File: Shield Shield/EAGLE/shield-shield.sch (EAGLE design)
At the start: 19 parts, among them IC1 MC33269D-5.0, J1 POWER_JACKSLT, U1 TXB0108PWR, U2 TXB0108PWR

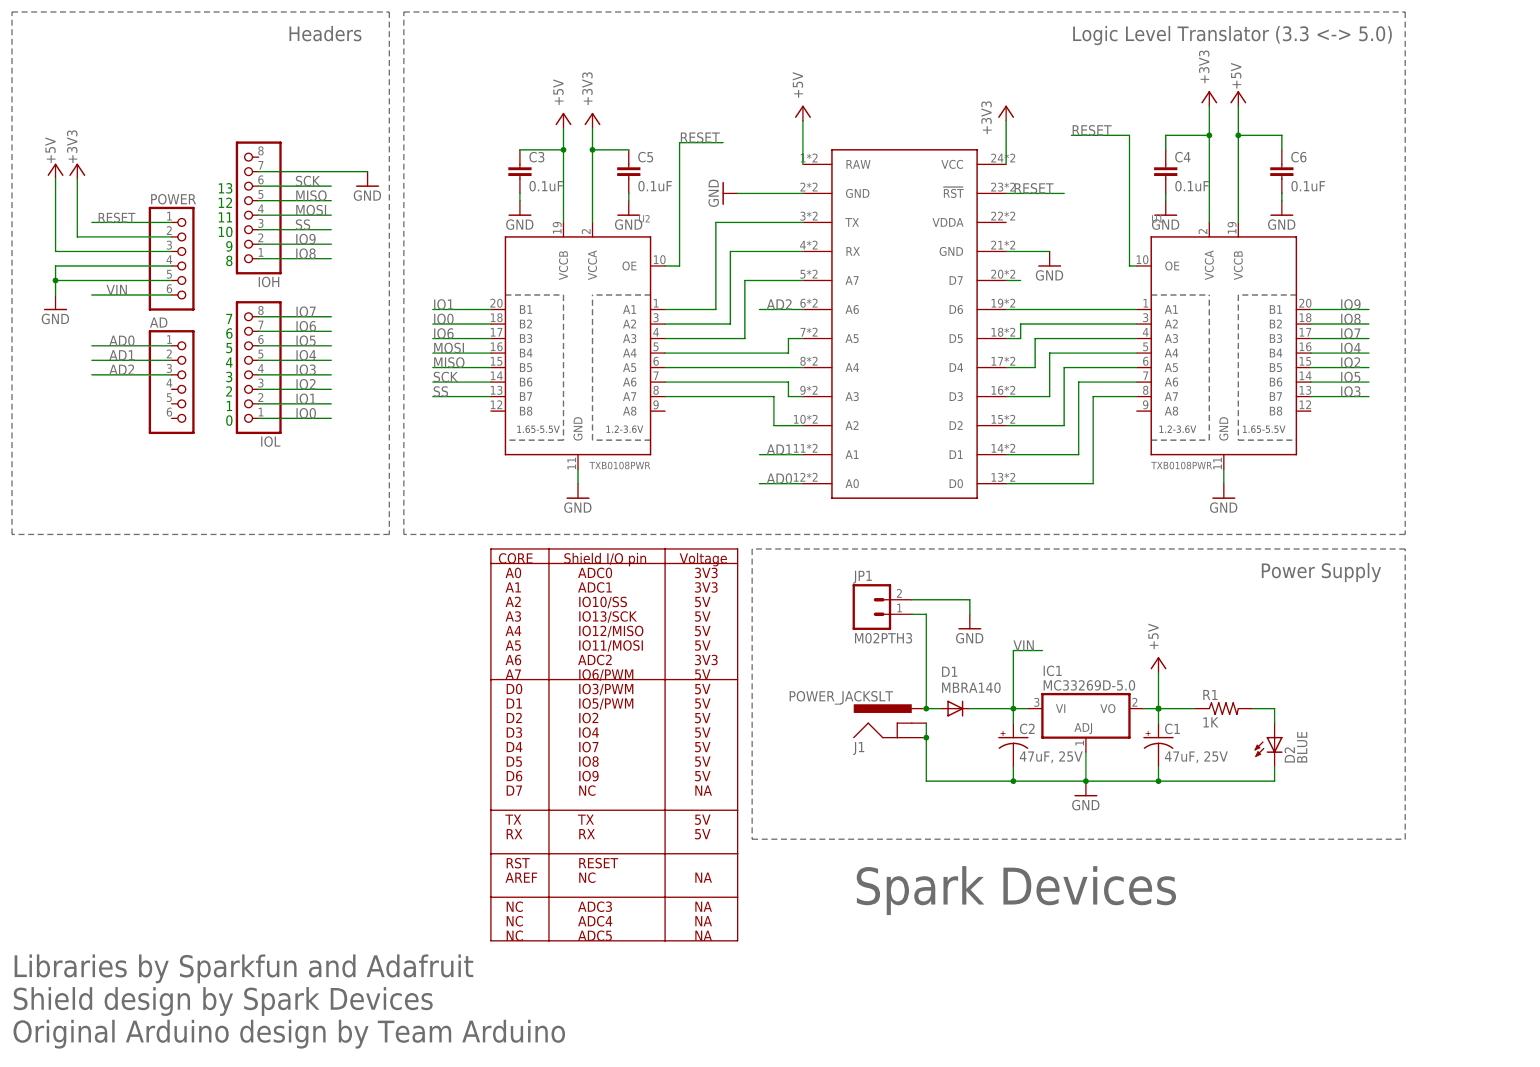
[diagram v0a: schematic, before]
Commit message: updated shield BOMs and boards
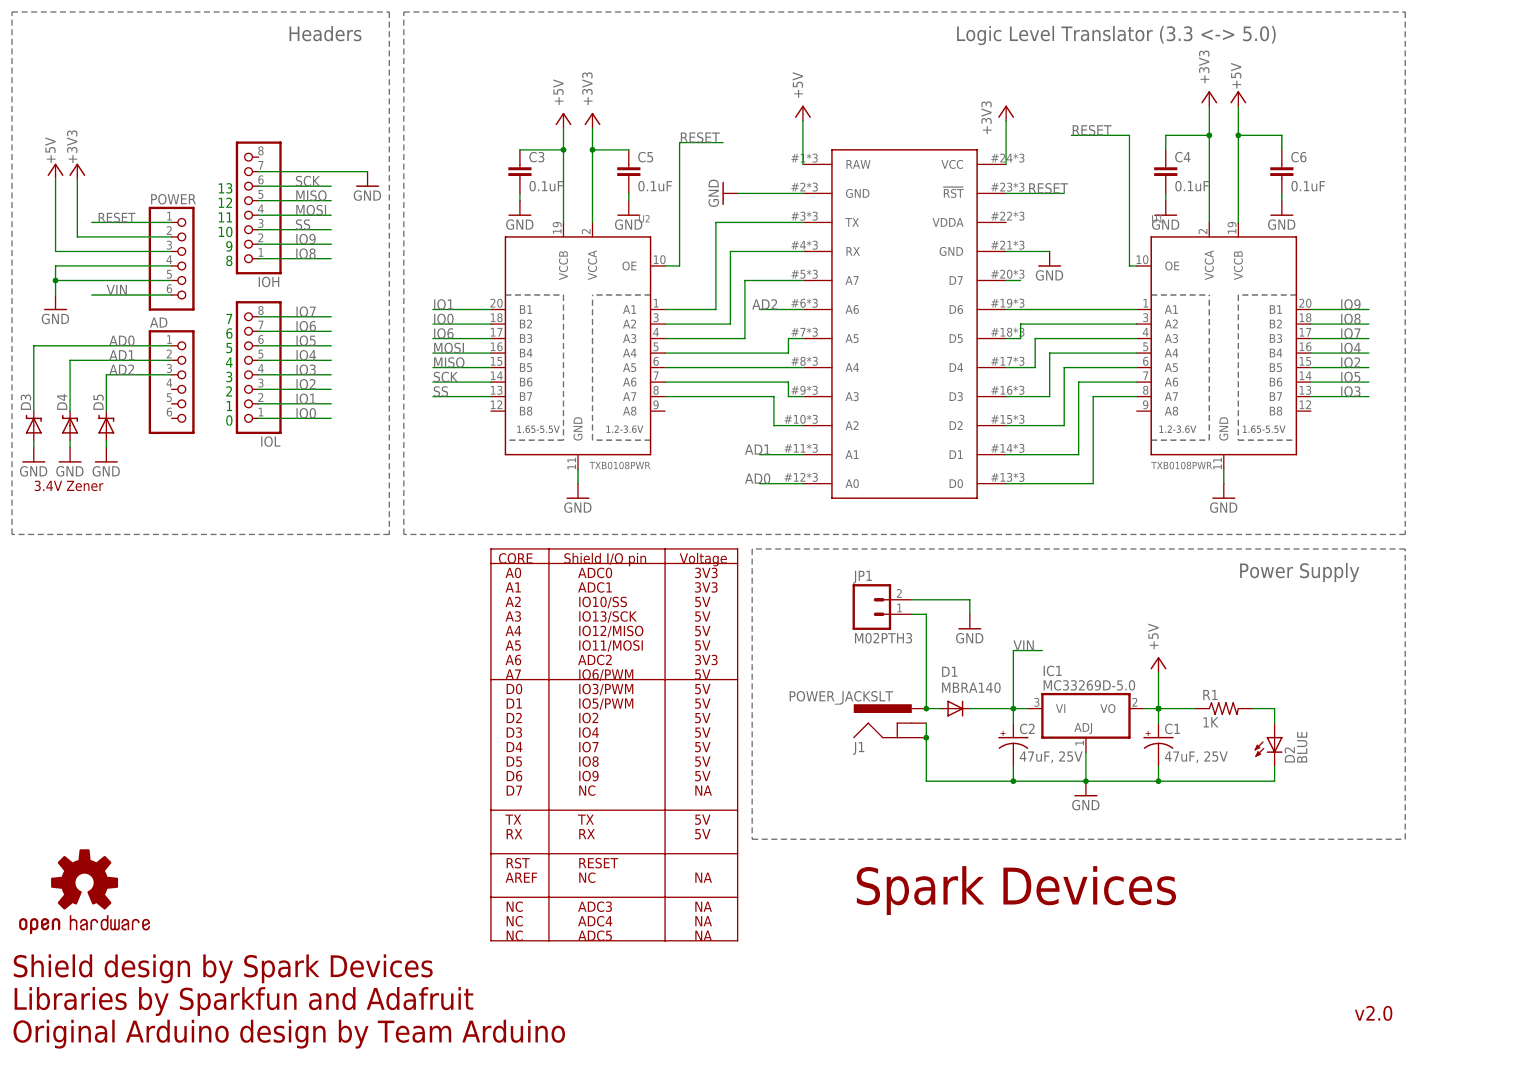
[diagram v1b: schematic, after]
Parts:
- added D3, D4, D5: DIODE-ZENER-BZT52, SparkFun-DiscreteSemi:DIODE-ZENER-BZT52
- added LOGO1: OSHW-LOGOM, Spark:OSHW-LOGOM
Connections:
- net AD0: now also D3.C
- net AD1: now also D4.C
- net AD2: now also D5.C
- net GND: now also D3.A, D4.A, D5.A
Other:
- note added: "3.4V Zener"
- note added: "Shield design by Spark Devices Libraries by Sparkfun and Adafruit Original Arduino design by Team Arduino"
- note added: "v2.0"
- note removed: "Libraries by Sparkfun and Adafruit Shield design by Spark Devices Original Arduino design by Team Arduino"
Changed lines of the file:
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@@
 <layer number="95" name="Names" color="7" fill="1" visible="yes" active="yes"/>
 <layer number="96" name="Values" color="7" fill="1" visible="yes" active="yes"/>
-<layer number="97" name="Info" color="7" fill="1" visible="no" active="yes"/>
+<layer number="97" name="Info" color="7" fill="1" visible="yes" active="yes"/>
 <layer number="98" name="Guide" color="6" fill="1" visible="no" active="yes"/>
 <layer number="100" name="Muster" color="7" fill="1" visible="no" active="yes"/>
@@
 <layer number="112" name="tSilk" color="7" fill="1" visible="yes" active="yes"/>
 <layer number="116" name="Patch_BOT" color="7" fill="1" visible="no" active="yes"/>
-<layer number="121" name="_tsilk" color="7" fill="1" visible="no" active="yes"/>
+<layer number="121" name="_tsilk" color="7" fill="1" visible="yes" active="yes"/>
 <layer number="122" name="_bsilk" color="7" fill="1" visible="no" active="yes"/>
 <layer number="123" name="tTestmark" color="7" fill="1" visible="no" active="yes"/>
@@
 <part name="JP1" library="SparkFun-Connectors" deviceset="M02" device="PTH3"/>
 <part name="GND11" library="supply1" deviceset="GND" device=""/>
+<part name="LOGO1" library="Spark" deviceset="OSHW-LOGO" device="M"/>
+<part name="D3" library="SparkFun-DiscreteSemi" deviceset="DIODE-ZENER" device="-BZT52"/>
+<part name="D4" library="SparkFun-DiscreteSemi" deviceset="DIODE-ZENER" device="-BZT52"/>
+<part name="D5" library="SparkFun-DiscreteSemi" deviceset="DIODE-ZENER" device="-BZT52"/>
+<part name="GND12" library="supply1" deviceset="GND" device=""/>
+<part name="GND13" library="supply1" deviceset="GND" device=""/>
+<part name="GND15" library="supply1" deviceset="GND" device=""/>
 </parts>
 <sheets>
@@
 <text x="41.275" y="148.59" size="1.778" layer="91" rot="MR0">12</text>
 <text x="41.275" y="151.13" size="1.778" layer="91" rot="MR0">13</text>
-<text x="149.86" y="26.67" size="6.4516" layer="95">Spark Devices</text>
+<text x="149.86" y="26.67" size="6.4516" layer="94" font="vector">Spark Devices</text>
 <wire x1="2.54" y1="182.88" x2="68.58" y2="182.88" width="0.2032" layer="95" style="dashdot"/>
 <wire x1="68.58" y1="182.88" x2="68.58" y2="91.44" width="0.2032" layer="95" style="dashdot"/>
@@
 <wire x1="132.08" y1="38.1" x2="246.38" y2="38.1" width="0.2032" layer="95" style="dashdot"/>
 <wire x1="246.38" y1="38.1" x2="246.38" y2="88.9" width="0.2032" layer="95" style="dashdot"/>
-<text x="220.98" y="83.82" size="2.54" layer="95">Power Supply</text>
-<text x="187.96" y="177.8" size="2.54" layer="95">Logic Level Translator (3.3 &lt;-&gt; 5.0)</text>
-<text x="50.8" y="177.8" size="2.54" layer="95">Headers</text>
-<text x="2.54" y="2.54" size="3.81" layer="95">Libraries by Sparkfun and Adafruit
-Shield design by Spark Devices
+<text x="217.17" y="83.82" size="2.54" layer="95" font="vector">Power Supply</text>
+<text x="167.64" y="177.8" size="2.54" layer="95" font="vector">Logic Level Translator (3.3 &lt;-&gt; 5.0)</text>
+<text x="50.8" y="177.8" size="2.54" layer="95" font="vector">Headers</text>
+<text x="2.54" y="2.54" size="3.81" layer="94" font="vector">Shield design by Spark Devices
+Libraries by Sparkfun and Adafruit
 Original Arduino design by Team Arduino</text>
 <wire x1="86.36" y1="88.9" x2="86.36" y2="86.36" width="0.2032" layer="94"/>
@@
 <text x="121.92" y="30.48" size="1.778" layer="94">NA</text>
 <wire x1="86.36" y1="27.94" x2="129.54" y2="27.94" width="0.2032" layer="94"/>
+<text x="6.35" y="99.06" size="1.778" layer="94" font="vector">3.4V Zener</text>
+<text x="237.49" y="6.35" size="2.54" layer="94" font="vector">v2.0</text>
 </plain>
 <instances>
@@
 <instance part="GND6" gate="1" x="224.79" y="147.32"/>
 <instance part="J1" gate="G$1" x="160.02" y="53.34" smashed="yes">
-<attribute name="VALUE" x="138.43" y="62.23" size="1.778" layer="96"/>
+<attribute name="VALUE" x="138.43" y="62.23" size="1.778" layer="96" font="vector"/>
 <attribute name="NAME" x="149.86" y="53.34" size="1.778" layer="95"/>
 </instance>
@@
 <instance part="JP1" gate="G$1" x="152.4" y="77.47"/>
 <instance part="GND11" gate="1" x="170.18" y="74.93"/>
+<instance part="LOGO1" gate="G$1" x="15.24" y="30.48"/>
+<instance part="D3" gate="G$1" x="6.35" y="110.49" smashed="yes" rot="R90">
+<attribute name="NAME" x="5.8674" y="113.03" size="1.778" layer="95" rot="R90"/>
+<attribute name="VALUE" x="8.6614" y="113.03" size="1.778" layer="96" rot="R90" display="off"/>
+</instance>
+<instance part="D4" gate="G$1" x="12.7" y="110.49" smashed="yes" rot="R90">
+<attribute name="NAME" x="12.2174" y="113.03" size="1.778" layer="95" rot="R90"/>
+<attribute name="VALUE" x="15.0114" y="113.03" size="1.778" layer="96" rot="R90" display="off"/>
+</instance>
+<instance part="D5" gate="G$1" x="19.05" y="110.49" smashed="yes" rot="R90">
+<attribute name="NAME" x="18.5674" y="113.03" size="1.778" layer="95" rot="R90"/>
+<attribute name="VALUE" x="21.3614" y="113.03" size="1.778" layer="96" rot="R90" display="off"/>
+</instance>
+<instance part="GND12" gate="1" x="19.05" y="104.14"/>
+<instance part="GND13" gate="1" x="12.7" y="104.14"/>
+<instance part="GND15" gate="1" x="6.35" y="104.14"/>
 </instances>
 <busses>
@@
 <pinref part="GND11" gate="1" pin="GND"/>
 </segment>
+<segment>
+<pinref part="D5" gate="G$1" pin="A"/>
+<pinref part="GND12" gate="1" pin="GND"/>
+<wire x1="19.05" y1="106.68" x2="19.05" y2="107.95" width="0.1524" layer="91"/>
+</segment>
+<segment>
+<pinref part="D4" gate="G$1" pin="A"/>
+<pinref part="GND13" gate="1" pin="GND"/>
+<wire x1="12.7" y1="107.95" x2="12.7" y2="106.68" width="0.1524" layer="91"/>
+</segment>
+<segment>
+<pinref part="D3" gate="G$1" pin="A"/>
+<pinref part="GND15" gate="1" pin="GND"/>
+<wire x1="6.35" y1="107.95" x2="6.35" y2="106.68" width="0.1524" layer="91"/>
+</segment>
 </net>
 <net name="RESET" class="0">
@@
 <pinref part="U$1" gate="G$1" pin="!RST"/>
 <wire x1="176.53" y1="151.13" x2="186.69" y2="151.13" width="0.1524" layer="91"/>
-<label x="177.8" y="151.13" size="1.778" layer="95"/>
+<label x="180.34" y="151.13" size="1.778" layer="95"/>
 </segment>
 <segment>
@@
 <net name="AD0" class="0">
 <segment>
-<wire x1="30.48" y1="124.46" x2="16.51" y2="124.46" width="0.1524" layer="91"/>
+<wire x1="30.48" y1="124.46" x2="6.35" y2="124.46" width="0.1524" layer="91"/>
 <label x="24.13" y="124.46" size="1.778" layer="95" rot="MR0"/>
 <pinref part="AD" gate="A" pin="1"/>
+<pinref part="D3" gate="G$1" pin="C"/>
+<wire x1="6.35" y1="124.46" x2="6.35" y2="113.03" width="0.1524" layer="91"/>
 </segment>
 <segment>
 <pinref part="U$1" gate="G$1" pin="A0"/>
 <wire x1="140.97" y1="100.33" x2="133.35" y2="100.33" width="0.1524" layer="91"/>
-<label x="134.62" y="100.33" size="1.778" layer="95"/>
+<label x="130.81" y="100.33" size="1.778" layer="95"/>
 </segment>
 </net>
@@
 <label x="24.13" y="121.92" size="1.778" layer="95" rot="MR0"/>
 <pinref part="AD" gate="A" pin="2"/>
-<wire x1="16.51" y1="121.92" x2="30.48" y2="121.92" width="0.1524" layer="91"/>
+<wire x1="12.7" y1="121.92" x2="30.48" y2="121.92" width="0.1524" layer="91"/>
+<pinref part="D4" gate="G$1" pin="C"/>
+<wire x1="12.7" y1="121.92" x2="12.7" y2="113.03" width="0.1524" layer="91"/>
 </segment>
 <segment>
 <pinref part="U$1" gate="G$1" pin="A1"/>
 <wire x1="140.97" y1="105.41" x2="133.35" y2="105.41" width="0.1524" layer="91"/>
-<label x="134.62" y="105.41" size="1.778" layer="95"/>
+<label x="130.81" y="105.41" size="1.778" layer="95"/>
 </segment>
 </net>
 <net name="AD2" class="0">
 <segment>
-<wire x1="30.48" y1="119.38" x2="16.51" y2="119.38" width="0.1524" layer="91"/>
+<wire x1="30.48" y1="119.38" x2="19.05" y2="119.38" width="0.1524" layer="91"/>
 <label x="24.13" y="119.38" size="1.778" layer="95" rot="MR0"/>
 <pinref part="AD" gate="A" pin="3"/>
+<pinref part="D5" gate="G$1" pin="C"/>
+<wire x1="19.05" y1="119.38" x2="19.05" y2="113.03" width="0.1524" layer="91"/>
 </segment>
 <segment>
 <pinref part="U$1" gate="G$1" pin="A6"/>
 <wire x1="140.97" y1="130.81" x2="133.35" y2="130.81" width="0.1524" layer="91"/>
-<label x="134.62" y="130.81" size="1.778" layer="95"/>
-</segment>
-</net>
+<label x="132.08" y="130.81" size="1.778" layer="95"/>
+</segment>
+</net>
